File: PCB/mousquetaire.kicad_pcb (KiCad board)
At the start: 2 copper layers, 22 x 110 mm, 34 parts, among them J1 Sum2, J2 Sum3, J3 Sum1, J4 PWR, J5 SUM, J6 Mi, J7 M1, J8 M2, J9 M3, U1 TL072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

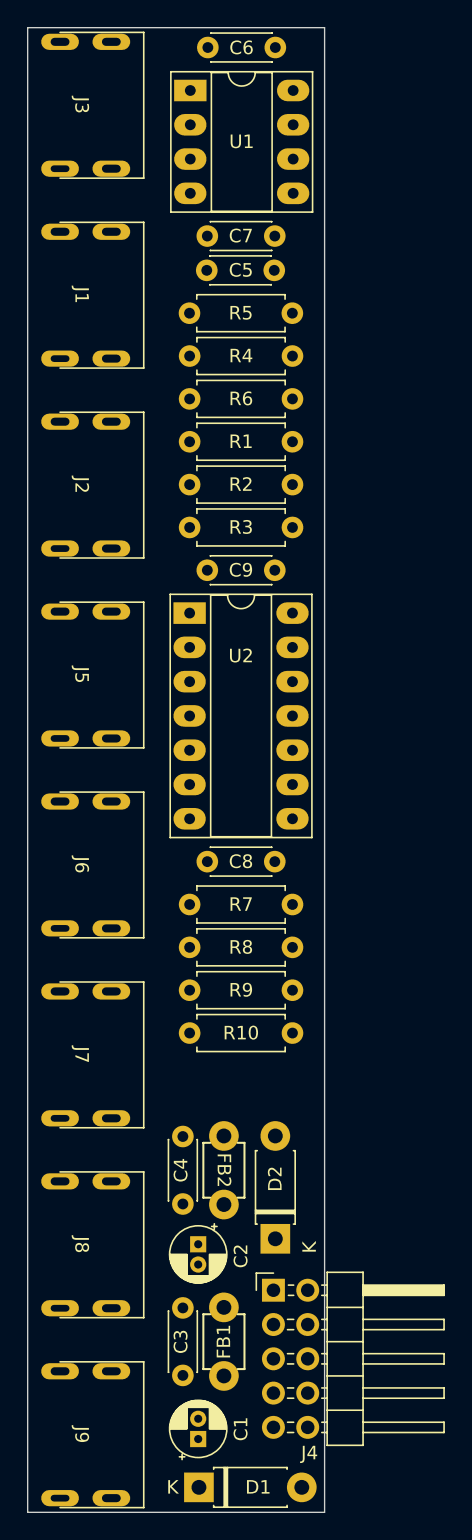
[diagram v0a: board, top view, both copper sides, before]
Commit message: :hammer: Adjust layout after fixing the schematic
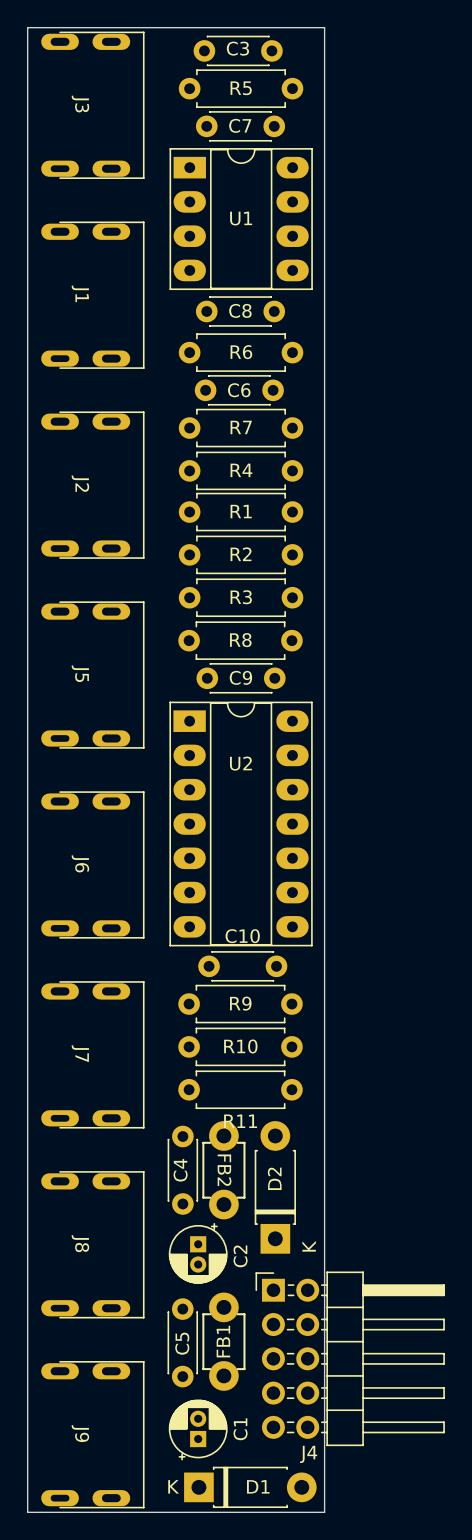
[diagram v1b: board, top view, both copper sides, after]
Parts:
- added C10: 100n, Capacitor_THT:C_Disc_D4.3mm_W1.9mm_P5.00mm, F.Cu at (128.4, 113.8)
- added R11: 1k, Resistor_THT:R_Axial_DIN0207_L6.3mm_D2.5mm_P7.62mm_Horizontal, F.Cu at (134.6, 122.9)
- C3, C6: value 100n -> 5p6
- C5: value 5p6 -> 100n
- R6, R8: value 1k -> 100k
- R7: value 100k -> 1k
- moved C3 93.4 mm to (133.1, 46.0), turned to 180 degrees
- moved C5 82.2 mm to (126.5, 144.2), turned to 90 degrees
- moved C8 41.1 mm to (133.3, 65.3), turned to 180 degrees
- moved R7 36.1 mm to (134.6, 73.9), turned to 180 degrees
- moved C6 25.4 mm to (133.2, 71.1)
- moved R8 24.0 mm to (127.0, 89.7), turned to 0 degrees
- moved R5 16.6 mm to (134.6, 48.8)
- moved R4 8.51 mm to (127.0, 77.1)
- moved C7 8.13 mm to (133.3, 51.6)
- moved C9 8.01 mm to (128.3, 92.5)
- moved U2 8.01 mm to (127.0, 95.6)
- moved U1 5.72 mm to (127.0, 54.6)
- moved R1 5.21 mm to (127.0, 80.1)
- moved R2 5.21 mm to (127.0, 83.3)
- moved R3 5.21 mm to (127.0, 86.5)
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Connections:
- C3 pad 1: +12V -> Net-(U1A--)
- C3 pad 2: GND -> Net-(C3-Pad2)
- C4 pad 1: GND -> +12V
- C4 pad 2: -12V -> GND
- C5 pad 1: Net-(U1B-+) -> GND
- C5 pad 2: SUM -> -12V
- C6 pad 1: +12V -> Net-(U1B--)
- C6 pad 2: GND -> SUM
- C7 pad 1: GND -> +12V
- C7 pad 2: -12V -> GND
- C8 pad 1: +12V -> GND
- C8 pad 2: GND -> -12V
- C9 pad 1: GND -> +12V
- C9 pad 2: -12V -> GND
- R1 pad 2: Net-(U1A-+) -> Net-(U1A--)
- R10 pad 1: Net-(U2C--) -> Net-(U2A--)
- R10 pad 2: Net-(J9-PadT) -> Net-(J8-PadT)
- R2 pad 2: Net-(U1A-+) -> Net-(U1A--)
- R3 pad 2: Net-(U1A-+) -> Net-(U1A--)
- R4 pad 1: Net-(R4-Pad1) -> Net-(C3-Pad2)
- R4 pad 2: Net-(U1B-+) -> Net-(U1B--)
- R5 pad 1: Net-(U1B-+) -> Net-(U1A--)
- R5 pad 2: SUM -> Net-(C3-Pad2)
- R6 pad 1: Net-(R6-Pad1) -> Net-(U1B--)
- R7 pad 1: Net-(J6-PadT) -> Net-(R7-Pad1)
- R7 pad 2: Net-(U2A-+) -> SUM
- R8 pad 1: Net-(U2A--) -> Net-(J6-PadT)
- R8 pad 2: Net-(J7-PadT) -> Net-(U2A-+)
- R9 pad 1: Net-(U2B--) -> Net-(U2C--)
- R9 pad 2: Net-(J8-PadT) -> Net-(J7-PadT)
- U1 pad 1: Net-(R4-Pad1) -> Net-(C3-Pad2)
- U1 pad 2: GND -> Net-(U1A--)
- U1 pad 3: Net-(U1A-+) -> GND
- U1 pad 5: Net-(U1B-+) -> GND
- U1 pad 6: GND -> Net-(U1B--)
- U1 pad 7: Net-(R6-Pad1) -> Net-(R7-Pad1)

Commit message: :sparkles: Route traces on the PCB
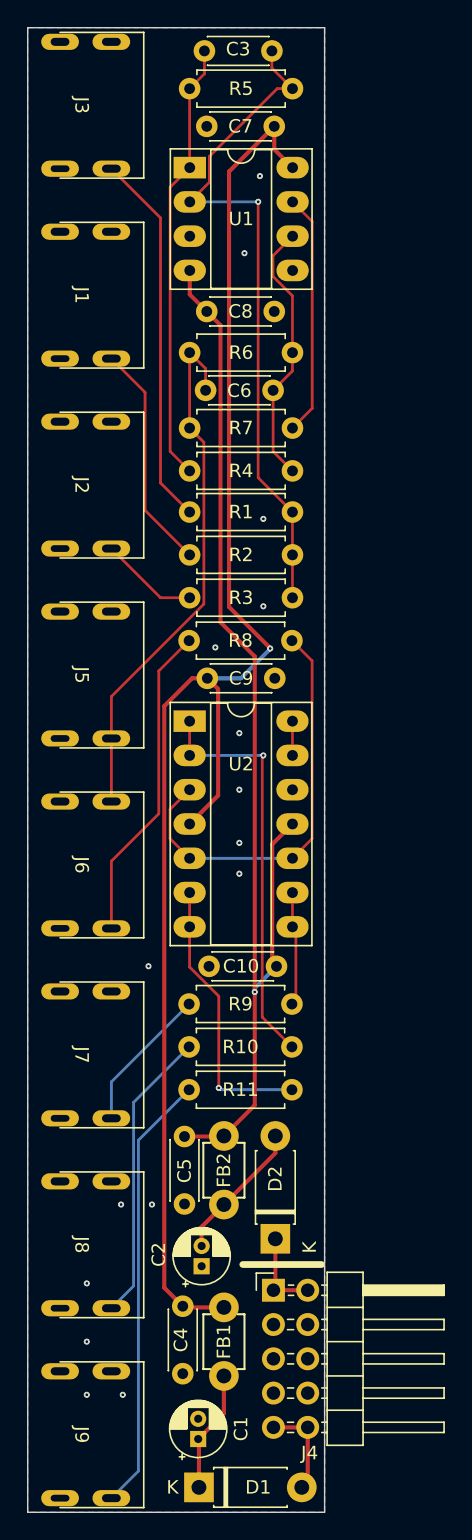
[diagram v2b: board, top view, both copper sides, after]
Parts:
- moved C5 12.8 mm to (126.6, 131.4)
- moved C4 12.6 mm to (126.5, 139.0)
- moved C2 1.65 mm to (127.9, 136.0), turned to 90 degrees
- turned FB2 to 90 degrees
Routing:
- net +12V: track 0.00 -> 114.7 mm, vias 0 -> 1
- net -12V: track 0.00 -> 83.9 mm, vias 0 -> 1
- net Net-(U1A--): track 0.00 -> 51.1 mm, vias 0 -> 1
- net SUM: track 0.00 -> 39.8 mm
- net Net-(C3-Pad2): track 0.00 -> 32.8 mm
- net Net-(J9-PadT): track 0.00 -> 32.6 mm
- net Net-(U2A-+): track 0.00 -> 31.2 mm
- net Net-(U2A--): track 0.00 -> 30.6 mm, vias 0 -> 1
- net Net-(J3-PadT): track 0.00 -> 27.8 mm
- net Net-(J6-PadT): track 0.00 -> 23.7 mm
- net Net-(J8-PadT): track 0.00 -> 21.7 mm
- net Net-(U2B--): track 0.00 -> 20.8 mm, vias 0 -> 1
- net Net-(U1B--): track 0.00 -> 19.8 mm
- net Net-(R7-Pad1): track 0.00 -> 18.0 mm
- net Net-(J1-PadT): track 0.00 -> 16.9 mm
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- added copper zone on B.Cu, net GND
- added copper zone on F.Cu, net GND
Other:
- board text added: "-12V"
- board text added: "https://github.com/moPsy-project/mousquetaire v1"

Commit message: :hammer: Turn power connector around and adapt to footprint
Move the power connector so that the red stripe is down.
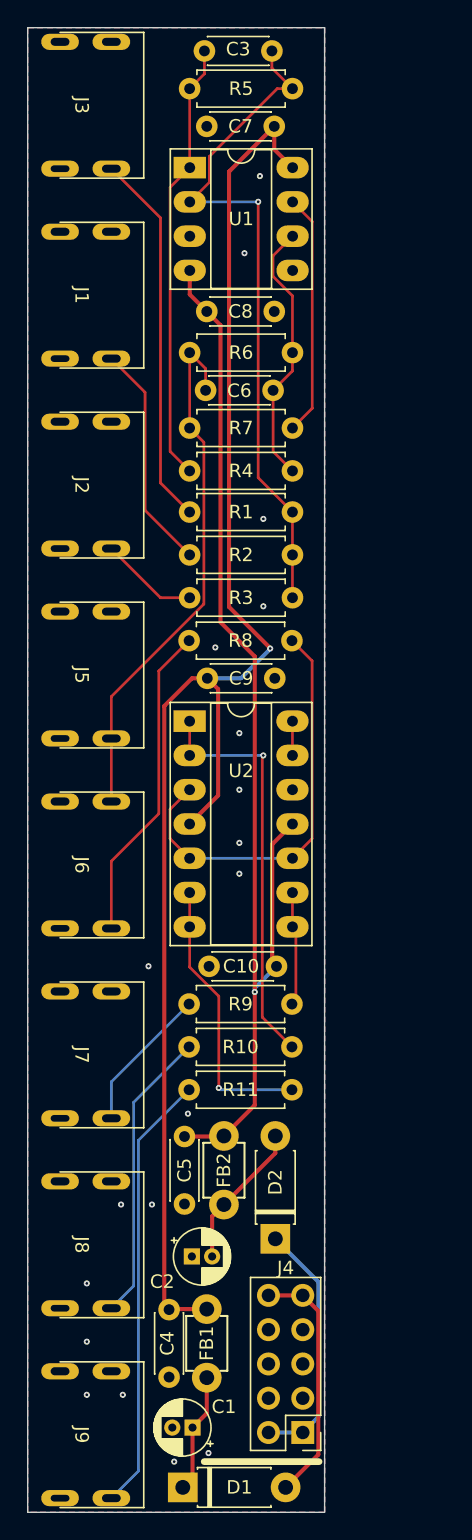
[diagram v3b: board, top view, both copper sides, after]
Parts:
- J4: footprint Connector_PinHeader_2.54mm:PinHeader_2x05_P2.54mm_Horizontal -> Connector_PinHeader_2.54mm:PinHeader_2x05_P2.54mm_Vertical
- moved J4 10.8 mm to (135.4, 148.3), turned to 180 degrees
- moved FB1 1.28 mm to (128.3, 141.7)
- moved D1 1.20 mm to (126.5, 152.4)
- moved C4 1.05 mm to (125.5, 139.2)
- moved C2 1.02 mm to (127.2, 135.3), turned to 0 degrees
- moved C1 0.95 mm to (127.2, 148.0), turned to 180 degrees
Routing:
- net Net-(D2-K): track 6.41 -> 18.7 mm
- net Net-(D1-A): track 7.17 -> 18.2 mm
- net GND: vias 16 -> 19
